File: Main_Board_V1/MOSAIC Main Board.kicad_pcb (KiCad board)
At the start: 2 copper layers, 89 x 92 mm, 79 parts, among them J1 CONN E, J10 QWIIC_RIGHT_ANGLE, J11 Vertical Qwiic Connector, J12 CONN E, J13 CONN E, J14 35RAPC4BH3 CONN 3.5MM, J2 CONN E, J3 CONN E, J4 CONN HEADER VERT 10POS 1.27MM, J5 USB TYPE C R/A SMT 16PIN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

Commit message: Update MOSAIC Main Board.kicad_pcb
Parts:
- moved R7 2.52 mm to (175.8, 78.7)
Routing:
- net 3.3V_QWIIC: track 15.1 -> 17.8 mm
- net Net-(D3-PadA): track 22.6 -> 24.2 mm
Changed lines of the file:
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@@
   )
   (footprint "main_board_footprints_V1.0:0603" (layer "F.Cu")
-    (at 178.25 78.1)
+    (at 175.8 78.7)
     (descr "<p><b>Generic 1608 (0603) package</b></p>\n<p>0.2mm courtyard excess rounded to nearest 0.05mm.</p>")
     (property "Field4" "https://www.digikey.com/en/products/detail/stackpole-electronics-inc/RMCF0603FT1K00/1761077")
@@
   (segment (start 186.8709 78.1209) (end 187.05 78.3) (width 0.5588) (layer "F.Cu") (net 8))
   (segment (start 187.05 78.3) (end 187.05 82.05) (width 0.5588) (layer "F.Cu") (net 8))
+  (segment (start 177.2291 78.1209) (end 182.1084 78.1209) (width 0.5588) (layer "F.Cu") (net 8))
+  (segment (start 176.65 78.7) (end 177.2291 78.1209) (width 0.5588) (layer "F.Cu") (net 8))
   (segment (start 187.4791 82.5209) (end 187.5 82.5) (width 0.5588) (layer "F.Cu") (net 8))
-  (segment (start 182.0875 78.1) (end 182.1084 78.1209) (width 0.5588) (layer "F.Cu") (net 8))
-  (segment (start 179.1 78.1) (end 182.0875 78.1) (width 0.5588) (layer "F.Cu") (net 8))
   (segment (start 187.05 82.05) (end 187.5 82.5) (width 0.5588) (layer "F.Cu") (net 8))
   (segment (start 170.6025 97.730198) (end 170.6025 97.7525) (width 0.1778) (layer "F.Cu") (net 9))
@@
   (segment (start 116 93.15) (end 116.75 93.9) (width 0.15) (layer "F.Cu") (net 12))
   (segment (start 116.75 93.9) (end 120.45 93.9) (width 0.15) (layer "F.Cu") (net 12))
+  (segment (start 177.4 66.4039) (end 177.4 76.25) (width 0.1778) (layer "F.Cu") (net 13))
+  (segment (start 177.4 76.25) (end 174.95 78.7) (width 0.1778) (layer "F.Cu") (net 13))
   (segment (start 181.5607 60.596) (end 181.5567 60.6) (width 0.1778) (layer "F.Cu") (net 13))
-  (segment (start 180.1539 60.9106) (end 180.1539 63.65) (width 0.1778) (layer "F.Cu") (net 13))
-  (segment (start 177.4 66.4039) (end 177.4 78.1) (width 0.1778) (layer "F.Cu") (net 13))
-  (segment (start 183.7 60.596) (end 181.5607 60.596) (width 0.1778) (layer "F.Cu") (net 13))
   (segment (start 180.1539 63.65) (end 177.4 66.4039) (width 0.1778) (layer "F.Cu") (net 13))
+  (segment (start 183.7 60.596) (end 181.5607 60.596) (width 0.1778) (layer "F.Cu") (net 13))
+  (segment (start 180.1539 60.9106) (end 180.1539 63.65) (width 0.1778) (layer "F.Cu") (net 13))
   (segment (start 179.8433 60.6) (end 180.1539 60.9106) (width 0.1778) (layer "F.Cu") (net 13))
   (via (at 179.8433 60.6) (size 0.8) (drill 0.3048) (layers "F.Cu" "B.Cu") (net 13))

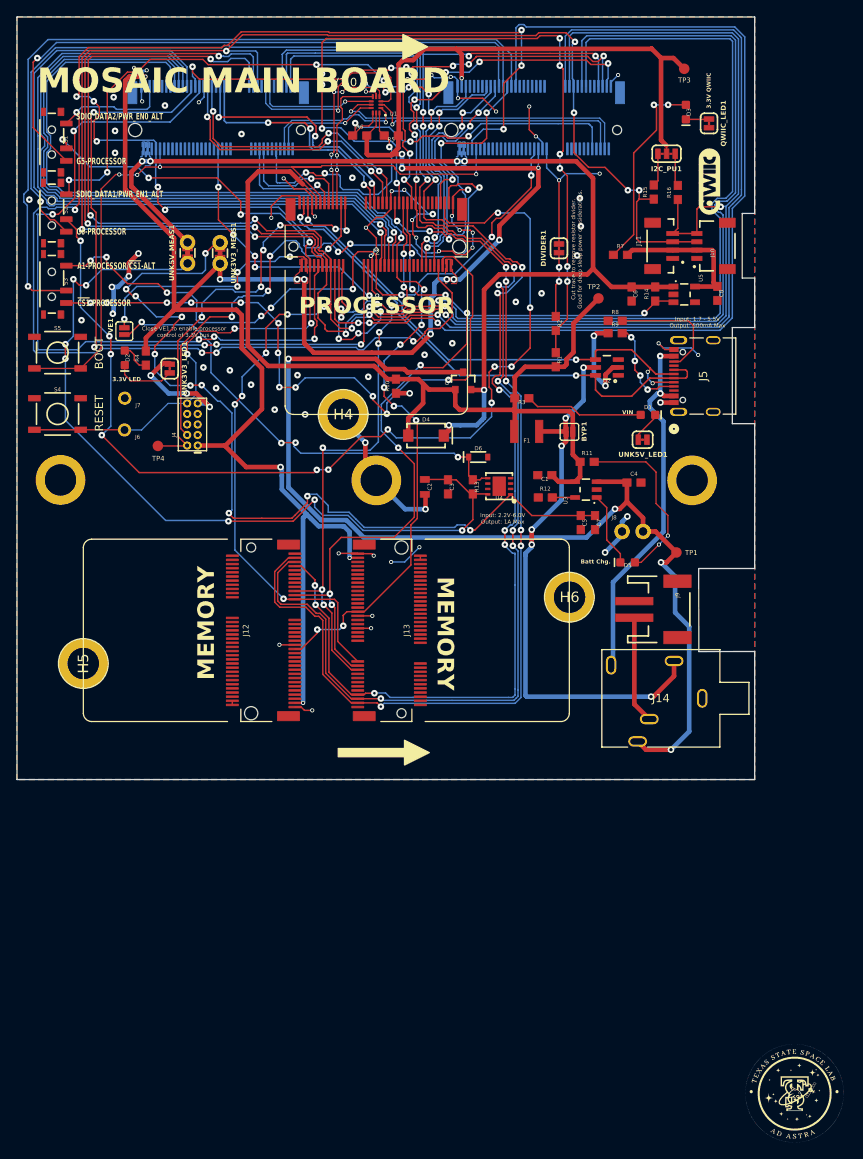
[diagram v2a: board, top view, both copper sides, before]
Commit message: Created board outline drawing
Created the outline drawing for the new, standardized, board outline.
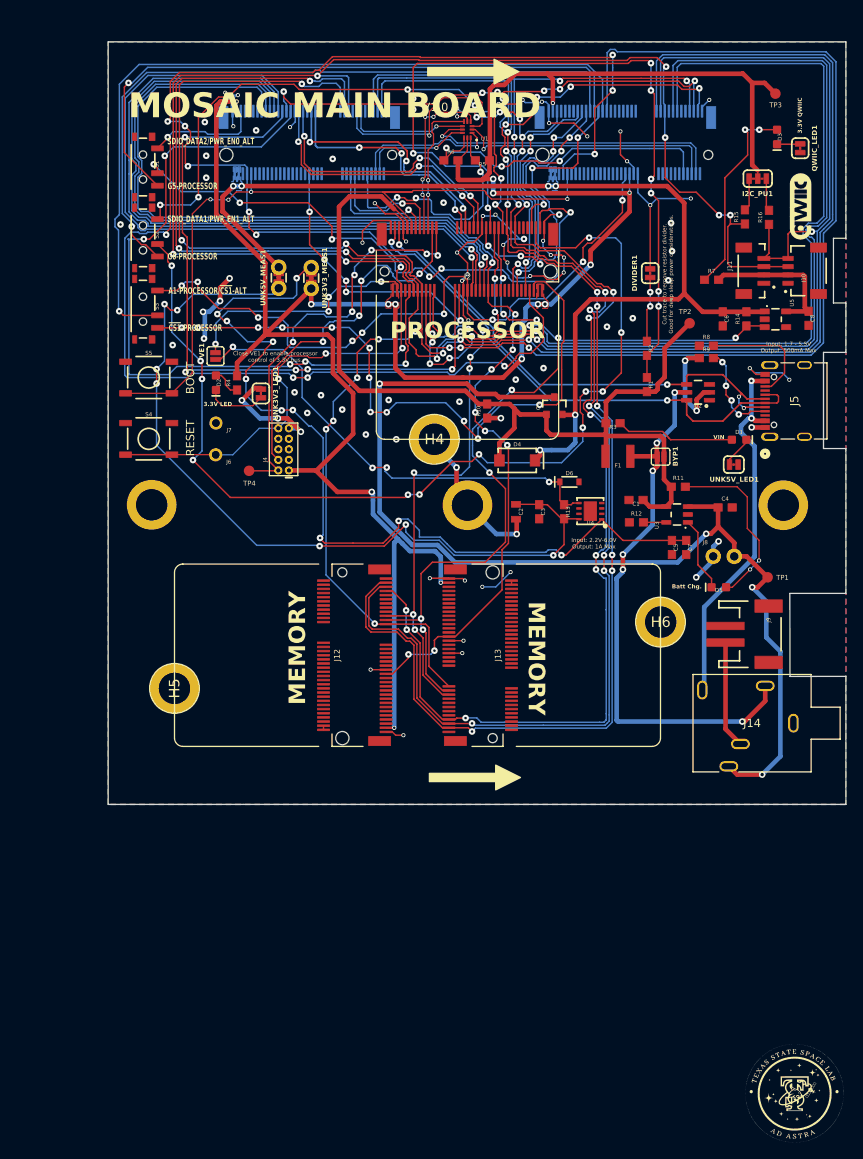
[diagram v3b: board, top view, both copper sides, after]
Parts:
- moved R4 11.4 mm to (129.6, 94.2)
- moved UNK5V_MEAS1 11.4 mm to (134.6, 81.5)
- moved QWIIC_LED1 11.4 mm to (197.5, 65.8)
- moved BYP1 11.4 mm to (180.7, 103.0)
- moved C1 11.4 mm to (177.7, 108.3)
- moved C2 11.4 mm to (163.2, 109.7)
- moved C3 11.4 mm to (166.0, 109.7)
- moved C4 11.4 mm to (188.4, 109.2)
- moved C5 11.4 mm to (182.0, 114.0)
- moved C6 11.4 mm to (188.2, 86.4)
- moved C7 11.4 mm to (183.7, 114.0)
- moved C8 11.4 mm to (198.5, 86.3)
- moved D1 11.4 mm to (190.1, 101.0)
- moved D2 11.4 mm to (127.0, 94.1)
- moved D3 11.4 mm to (194.7, 64.5)
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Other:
- outline, holes or cut-outs redrawn
